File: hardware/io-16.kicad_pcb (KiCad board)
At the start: 2 copper layers, 75 x 35 mm, 39 parts, among them J1 AKL_5_2, J10 AKL_5_2, J11 AKL_5_2, J12 AKL_5_2, J13 AKL_5_2, J2 AKL_5_2, J3 AKL_5_2, J4 AKL_5_2, J5 AKL_5_2, J6 AKL_5_2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

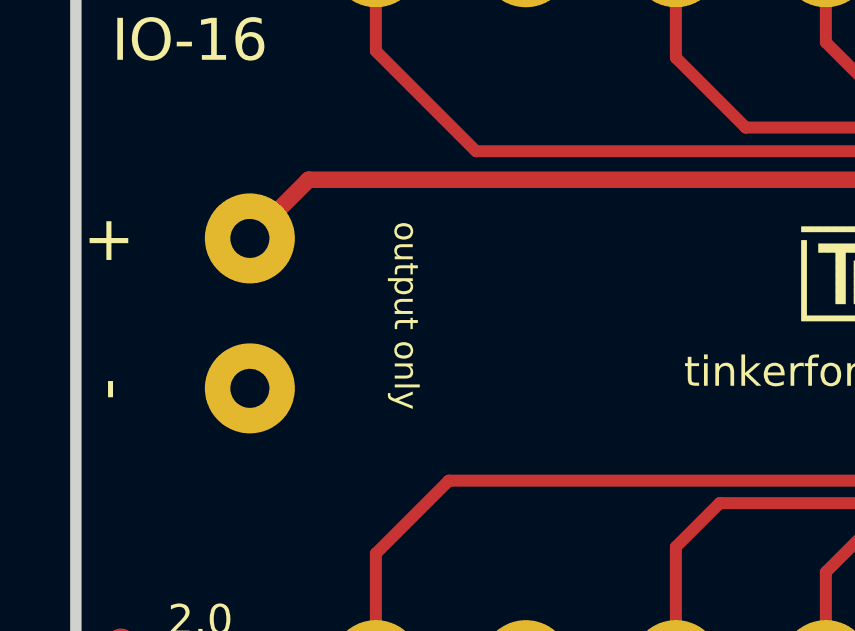
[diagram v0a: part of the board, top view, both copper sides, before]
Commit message: specify I2C pullup value
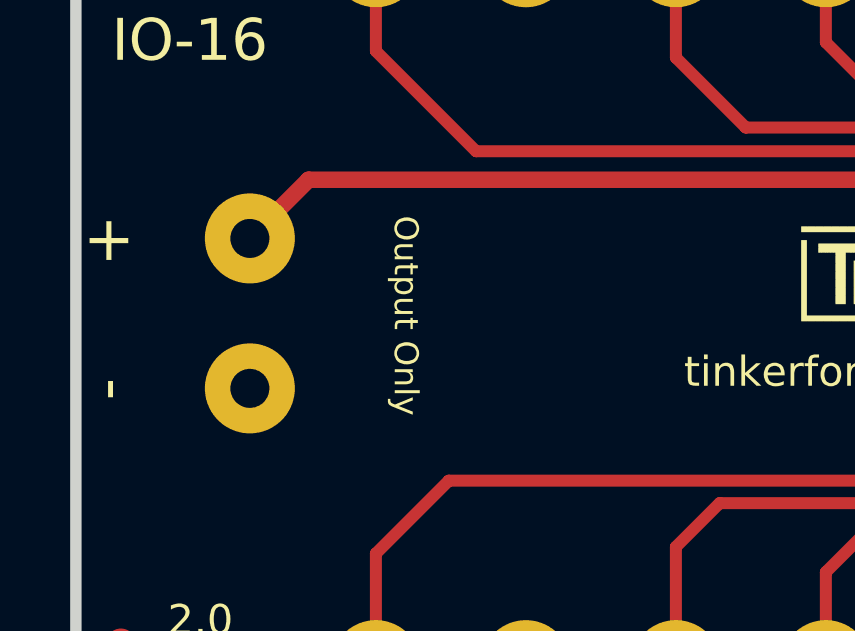
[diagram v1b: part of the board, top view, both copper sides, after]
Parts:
- RP1: value TBD -> 2k2
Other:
- board text added: "Output Only"
- board text removed: "output only"
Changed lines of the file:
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@@
-(kicad_pcb (version 4) (host pcbnew 4.0.2+dfsg1-stable)
+(kicad_pcb (version 4) (host pcbnew 4.0.7-e2-6376~58~ubuntu17.04.1)
   (general
     (links 81)
     (no_connects 0)
-    (area 111.309499 79.339499 186.690501 114.720501)
+    (area 15.62915 78.674999 187.355001 194.490793)
     (thickness 1.6002)
     (drawings 47)
@@
       (effects (font (size 0.29972 0.29972) (thickness 0.07493)))
     )
-    (fp_text value TBD (at 0.66 0 180) (layer F.Fab)
+    (fp_text value 2k2 (at 0.66 0 180) (layer F.Fab)
       (effects (font (size 0.29972 0.29972) (thickness 0.07493)))
     )
@@
     (effects (font (size 1.00076 1.00076) (thickness 0.14986)))
   )
-  (gr_text "output only" (at 122.49912 97.09912 270) (layer F.SilkS)
+  (gr_text "Output Only" (at 122.49912 97.09912 270) (layer F.SilkS)
     (effects (font (size 0.8001 0.8001) (thickness 0.14986)))
   )
